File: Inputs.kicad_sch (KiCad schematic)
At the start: 2 parts, among them J15 Digital Inputs

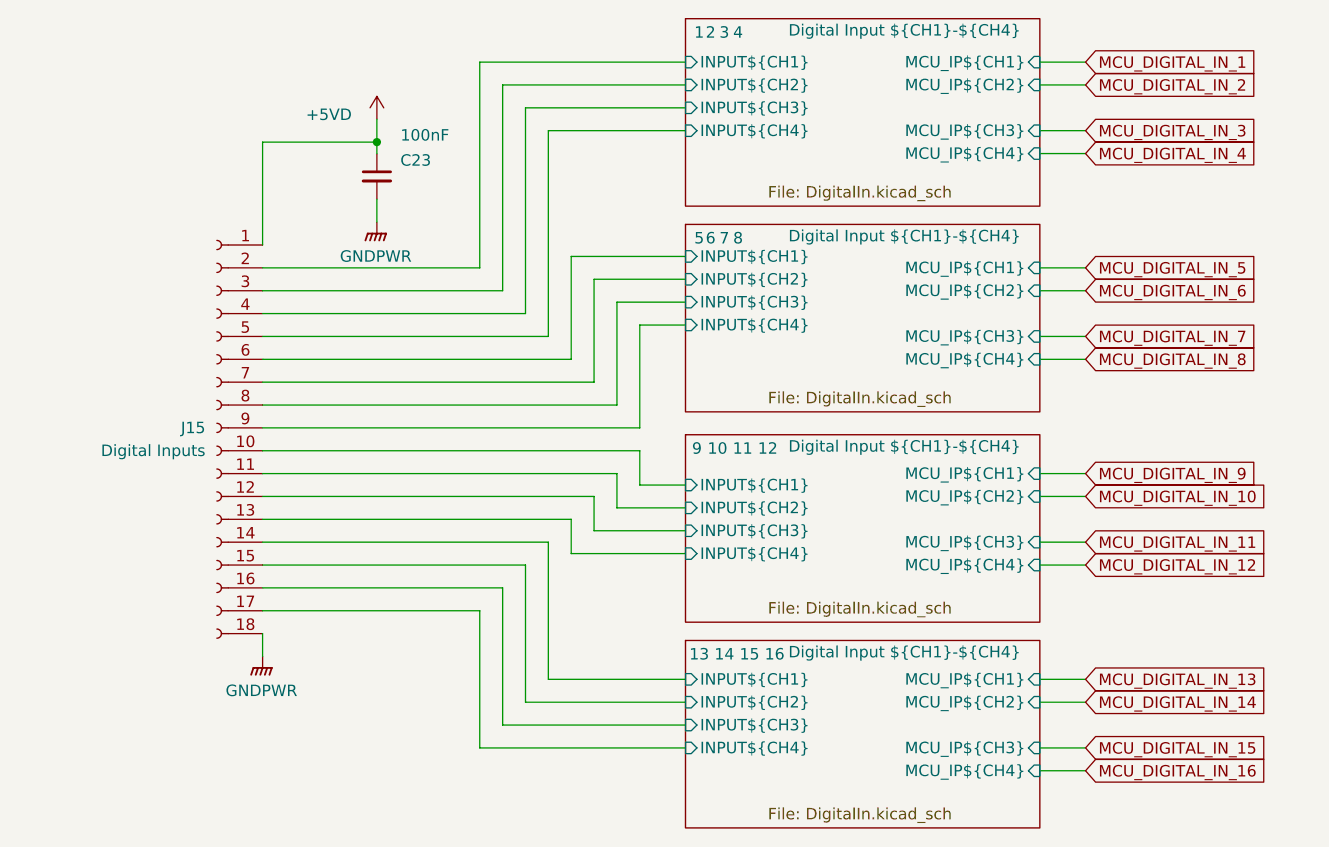
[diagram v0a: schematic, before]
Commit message: Renumbered IO to start at 0 to match firmware
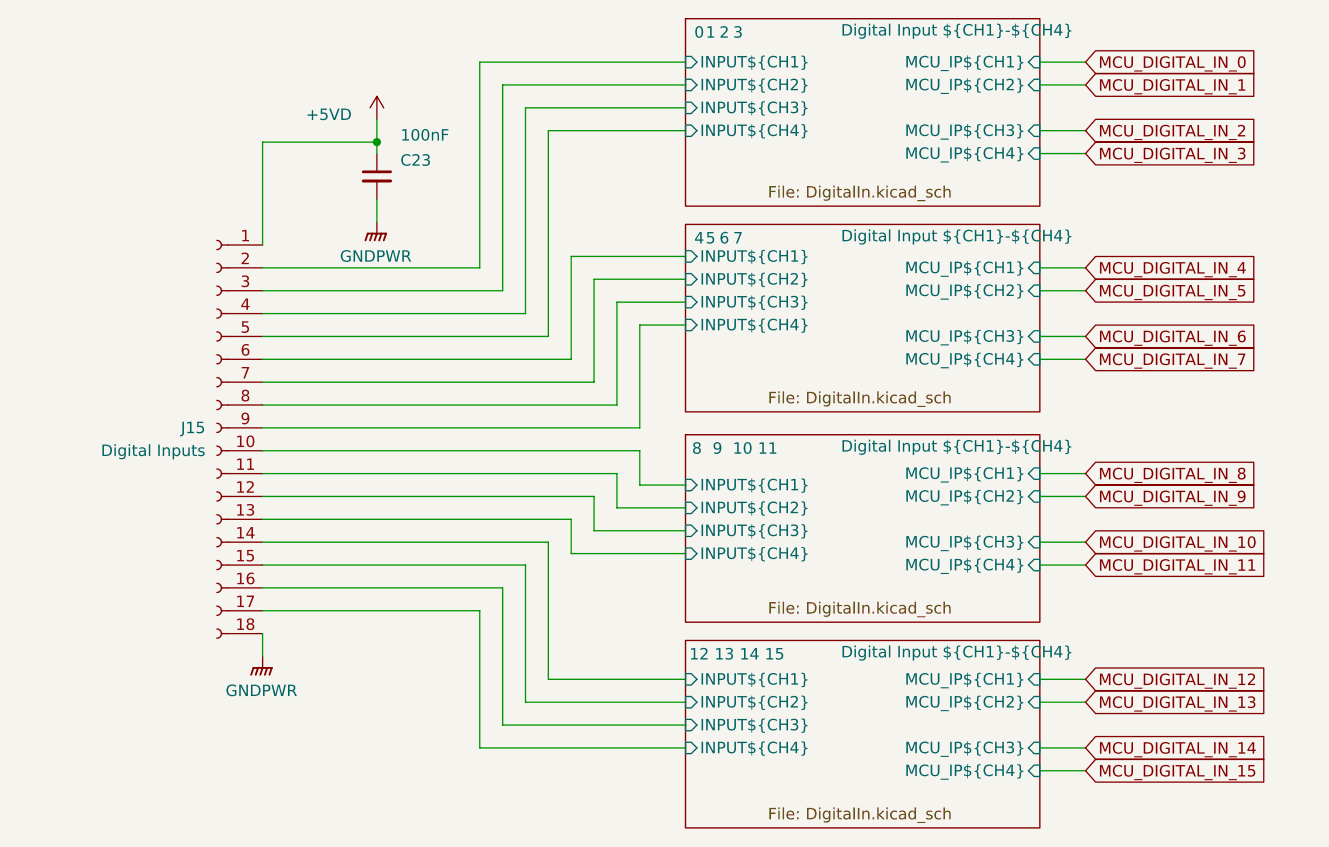
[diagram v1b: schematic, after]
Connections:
- net Digital Input ${CH1}-${CH4}/INPUT${CH1} is gone; now on net Digital Input ${CH1}-${CH4}/INPUT${CH1}: J15.6 (Pin_6)
- net Digital Input ${CH1}-${CH4}/INPUT${CH2} is gone; now on net Digital Input ${CH1}-${CH4}/INPUT${CH2}: J15.7 (Pin_7)
- net Digital Input ${CH1}-${CH4}/INPUT${CH3} is gone; now on net Digital Input ${CH1}-${CH4}/INPUT${CH3}: J15.8 (Pin_8)
- net Digital Input ${CH1}-${CH4}/INPUT${CH4} is gone; now on net Digital Input ${CH1}-${CH4}/INPUT${CH4}: J15.9 (Pin_9)
- net Digital Input ${CH1}-${CH4}/INPUT${CH1}: no longer J15.10 (Pin_10)
- net Digital Input ${CH1}-${CH4}/INPUT${CH2}: no longer J15.11 (Pin_11)
- net Digital Input ${CH1}-${CH4}/INPUT${CH3}: no longer J15.12 (Pin_12)
- net Digital Input ${CH1}-${CH4}/INPUT${CH4}: no longer J15.13 (Pin_13)
- new net Digital Input ${CH1}-${CH4}/INPUT${CH1}: J15.10 (Pin_10)
- new net Digital Input ${CH1}-${CH4}/INPUT${CH2}: J15.11 (Pin_11)
- new net Digital Input ${CH1}-${CH4}/INPUT${CH3}: J15.12 (Pin_12)
- new net Digital Input ${CH1}-${CH4}/INPUT${CH4}: J15.13 (Pin_13)

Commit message: more BOM consolidation. Switched out IO for vertical toolless wire to board terminals and added footprints. Put new isolated ground plane on board.
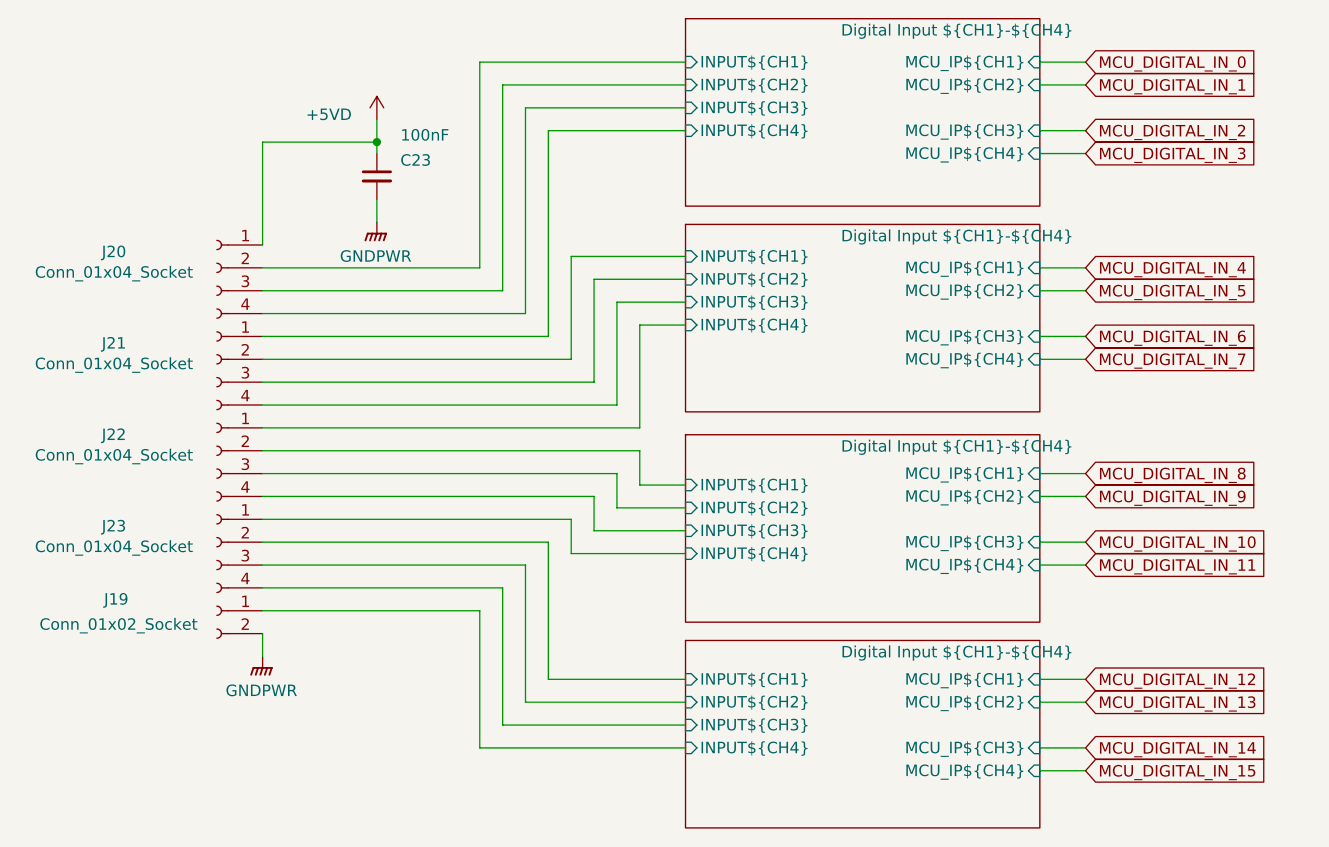
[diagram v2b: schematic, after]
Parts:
- removed J15: Digital Inputs, EBWA_06_A:CONN_EBWA-18-A_ADM, symbol Connector:Conn_01x18_Socket
- added J19: Conn_01x02_Socket, Amphenol QT:QT02ADP83V0000G, symbol Connector:Conn_01x02_Socket
- added J20, J21, J22, J23: Conn_01x04_Socket, Amphenol QT:QT04ADP83V0000G, symbol Connector:Conn_01x04_Socket
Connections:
- net +5VD: now also J20.1 (Pin_1)
- net Digital Input ${CH1}-${CH4}/INPUT${CH1}: now also J21.2 (Pin_2)
- net Digital Input ${CH1}-${CH4}/INPUT${CH2}: now also J21.3 (Pin_3)
- net Digital Input ${CH1}-${CH4}/INPUT${CH3}: now also J21.4 (Pin_4)
- net Digital Input ${CH1}-${CH4}/INPUT${CH4}: now also J21.1 (Pin_1)
- net GNDPWR: now also J19.2 (Pin_2)
- new net Digital Input ${CH1}-${CH4}/INPUT${CH1}: J23.2 (Pin_2)
- new net Digital Input ${CH1}-${CH4}/INPUT${CH1}: J20.2 (Pin_2)
- new net Digital Input ${CH1}-${CH4}/INPUT${CH1}: J22.2 (Pin_2)
- new net Digital Input ${CH1}-${CH4}/INPUT${CH2}: J23.3 (Pin_3)
- new net Digital Input ${CH1}-${CH4}/INPUT${CH2}: J20.3 (Pin_3)
- new net Digital Input ${CH1}-${CH4}/INPUT${CH2}: J22.3 (Pin_3)
- new net Digital Input ${CH1}-${CH4}/INPUT${CH3}: J23.4 (Pin_4)
- new net Digital Input ${CH1}-${CH4}/INPUT${CH3}: J20.4 (Pin_4)
- new net Digital Input ${CH1}-${CH4}/INPUT${CH3}: J22.4 (Pin_4)
- new net Digital Input ${CH1}-${CH4}/INPUT${CH4}: J23.1 (Pin_1)
- new net Digital Input ${CH1}-${CH4}/INPUT${CH4}: J19.1 (Pin_1)
- new net Digital Input ${CH1}-${CH4}/INPUT${CH4}: J22.1 (Pin_1)

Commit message: New PSU designs + footprints assigned. Changes to board shape to make room for new components. BOM consolidation of supplimentary file
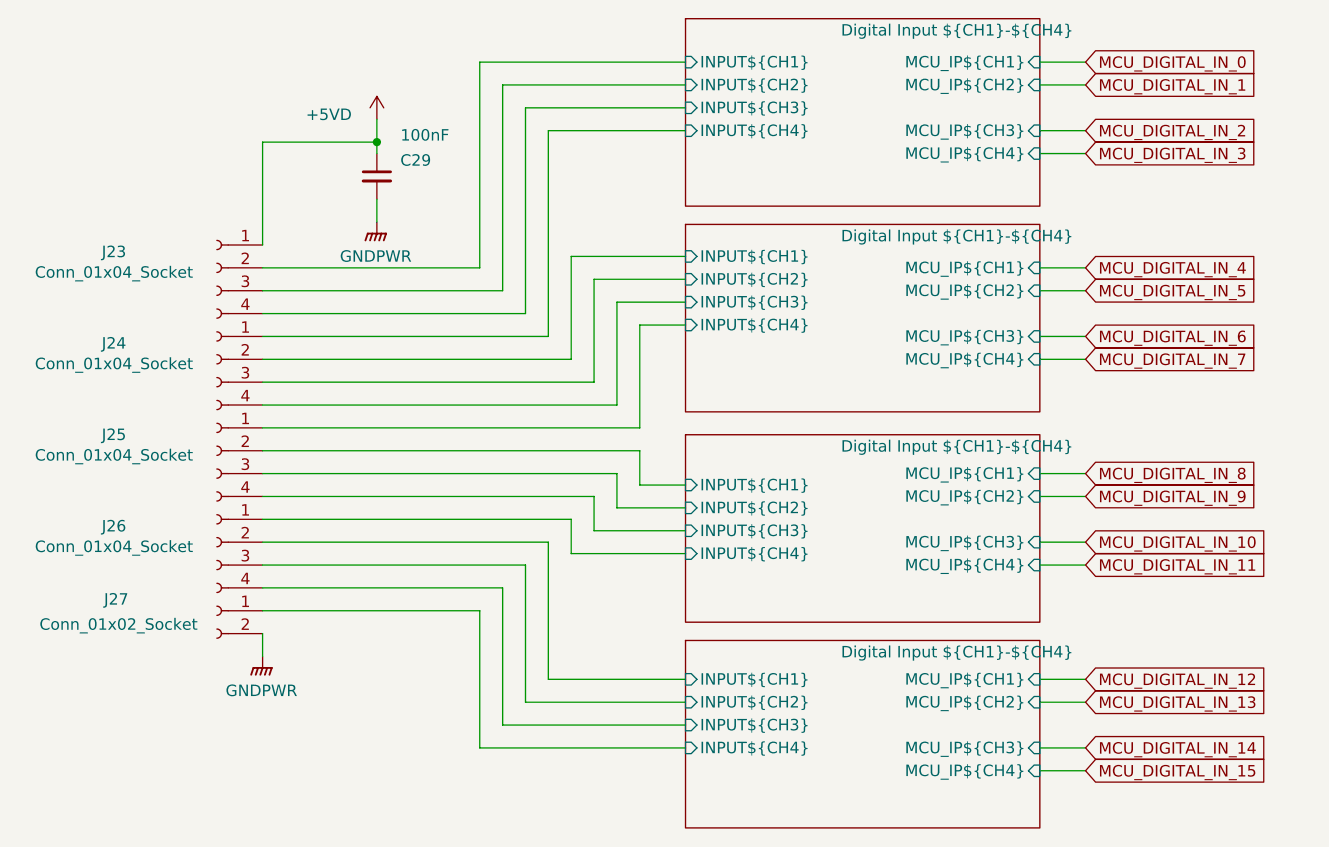
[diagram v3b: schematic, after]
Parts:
- J23: renamed from J20; Digikey Part Number 1818-QT02ADP83V0000G-ND -> 1818-QT04ADP83V0000G-ND; Digikey URL https://www.digikey.com.au/en/products/detail/amphenol-anytek/QT02ADP83V0000G/25618889 -> https://www.digikey.com.au/en/products/detail/amphenol-anytek/QT04ADP83V0000G/25618782
- J24: renamed from J21; Digikey Part Number 1818-QT02ADP83V0000G-ND -> 1818-QT04ADP83V0000G-ND; Digikey URL https://www.digikey.com.au/en/products/detail/amphenol-anytek/QT02ADP83V0000G/25618889 -> https://www.digikey.com.au/en/products/detail/amphenol-anytek/QT04ADP83V0000G/25618782
- J25: renamed from J22; Digikey Part Number 1818-QT02ADP83V0000G-ND -> 1818-QT04ADP83V0000G-ND; Digikey URL https://www.digikey.com.au/en/products/detail/amphenol-anytek/QT02ADP83V0000G/25618889 -> https://www.digikey.com.au/en/products/detail/amphenol-anytek/QT04ADP83V0000G/25618782
- J26: renamed from J23; Digikey Part Number 1818-QT02ADP83V0000G-ND -> 1818-QT04ADP83V0000G-ND; Digikey URL https://www.digikey.com.au/en/products/detail/amphenol-anytek/QT02ADP83V0000G/25618889 -> https://www.digikey.com.au/en/products/detail/amphenol-anytek/QT04ADP83V0000G/25618782
- J27: renamed from J19; Digikey Part Number 1818-QT04ADP83V0000G-ND -> 1818-QT02ADP83V0000G-ND; Digikey URL https://www.digikey.com.au/en/products/detail/amphenol-anytek/QT04ADP83V0000G/25618782 -> https://www.digikey.com.au/en/products/detail/amphenol-anytek/QT02ADP83V0000G/25618889
- renumbered C23 to C29
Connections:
- net Digital Input ${CH1}-${CH4}/INPUT${CH1} is gone; now on net Digital Input ${CH1}-${CH4}/INPUT${CH1}: J24.2 (Pin_2)
- net Digital Input ${CH1}-${CH4}/INPUT${CH2} is gone; now on net Digital Input ${CH1}-${CH4}/INPUT${CH2}: J24.3 (Pin_3)
- net Digital Input ${CH1}-${CH4}/INPUT${CH3} is gone; now on net Digital Input ${CH1}-${CH4}/INPUT${CH3}: J24.4 (Pin_4)
- net Digital Input ${CH1}-${CH4}/INPUT${CH4} is gone; now on net Digital Input ${CH1}-${CH4}/INPUT${CH4}: J24.1 (Pin_1)
- net Digital Input ${CH1}-${CH4}/INPUT${CH1}: no longer J26.2 (Pin_2)
- net Digital Input ${CH1}-${CH4}/INPUT${CH2}: no longer J26.3 (Pin_3)
- net Digital Input ${CH1}-${CH4}/INPUT${CH3}: no longer J26.4 (Pin_4)
- net Digital Input ${CH1}-${CH4}/INPUT${CH4}: no longer J26.1 (Pin_1)
- new net Digital Input ${CH1}-${CH4}/INPUT${CH1}: J26.2 (Pin_2)
- new net Digital Input ${CH1}-${CH4}/INPUT${CH2}: J26.3 (Pin_3)
- new net Digital Input ${CH1}-${CH4}/INPUT${CH3}: J26.4 (Pin_4)
- new net Digital Input ${CH1}-${CH4}/INPUT${CH4}: J26.1 (Pin_1)
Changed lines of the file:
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@@
 		(on_board yes)
 		(dnp no)
-		(property "Reference" "J23"
+		(property "Reference" "J26"
 			(at 80.01 104.902 0)
 			(effects
@@
 			)
 		)
-		(property "Digikey Part Number" "1818-QT02ADP83V0000G-ND"
+		(property "Digikey Part Number" "1818-QT04ADP83V0000G-ND"
 			(at 91.44 106.68 0)
 			(effects
@@
 			)
 		)
-		(property "Digikey URL" "https://www.digikey.com.au/en/products/detail/amphenol-anytek/QT02ADP83V0000G/25618889"
+		(property "Digikey URL" "https://www.digikey.com.au/en/products/detail/amphenol-anytek/QT04ADP83V0000G/25618782"
 			(at 91.44 106.68 0)
 			(effects
@@
 			(project "Remora Nucleo F446ZE Hat"
 				(path "/5473abc6-7b93-43cc-a401-f691c4d7d7cf/181d5939-8311-41b3-8216-f7233e3a75eb"
-					(reference "J23")
+					(reference "J26")
 					(unit 1)
 				)
@@
 		(dnp no)
 		(fields_autoplaced yes)
-		(property "Reference" "#PWR0133"
+		(property "Reference" "#PWR0202"
 			(at 96.52 124.46 0)
 			(effects
@@
 			(project "Remora Nucleo F446ZE Hat"
 				(path "/5473abc6-7b93-43cc-a401-f691c4d7d7cf/181d5939-8311-41b3-8216-f7233e3a75eb"
-					(reference "#PWR0133")
+					(reference "#PWR0202")
 					(unit 1)
 				)
@@
 		(on_board yes)
 		(dnp no)
-		(property "Reference" "#PWR0134"
+		(property "Reference" "#PWR0203"
 			(at 109.22 63.5 0)
 			(effects
@@
 			(project "Remora Nucleo F446ZE Hat"
 				(path "/5473abc6-7b93-43cc-a401-f691c4d7d7cf/181d5939-8311-41b3-8216-f7233e3a75eb"
-					(reference "#PWR0134")
+					(reference "#PWR0203")
 					(unit 1)
 				)
@@
 		(on_board yes)
 		(dnp no)
-		(property "Reference" "J20"
+		(property "Reference" "J23"
 			(at 80.01 74.422 0)
 			(effects
@@
 			)
 		)
-		(property "Digikey Part Number" "1818-QT02ADP83V0000G-ND"
+		(property "Digikey Part Number" "1818-QT04ADP83V0000G-ND"
 			(at 91.44 76.2 0)
 			(effects
@@
 			)
 		)
-		(property "Digikey URL" "https://www.digikey.com.au/en/products/detail/amphenol-anytek/QT02ADP83V0000G/25618889"
+		(property "Digikey URL" "https://www.digikey.com.au/en/products/detail/amphenol-anytek/QT04ADP83V0000G/25618782"
 			(at 91.44 76.2 0)
 			(effects
@@
 			(project "Remora Nucleo F446ZE Hat"
 				(path "/5473abc6-7b93-43cc-a401-f691c4d7d7cf/181d5939-8311-41b3-8216-f7233e3a75eb"
-					(reference "J20")
+					(reference "J23")
 					(unit 1)
 				)
@@
 		(on_board yes)
 		(dnp no)
-		(property "Reference" "C23"
+		(property "Reference" "C29"
 			(at 113.538 64.262 0)
 			(effects
@@
 			(project "Remora Nucleo F446ZE Hat"
 				(path "/5473abc6-7b93-43cc-a401-f691c4d7d7cf/181d5939-8311-41b3-8216-f7233e3a75eb"
-					(reference "C23")
+					(reference "C29")
 					(unit 1)
 				)
@@
 		(dnp no)
 		(fields_autoplaced yes)
-		(property "Reference" "#PWR0135"
+		(property "Reference" "#PWR0204"
 			(at 109.22 76.2 0)
 			(effects
@@
 			(project "Remora Nucleo F446ZE Hat"
 				(path "/5473abc6-7b93-43cc-a401-f691c4d7d7cf/181d5939-8311-41b3-8216-f7233e3a75eb"
-					(reference "#PWR0135")
+					(reference "#PWR0204")
 					(unit 1)
 				)
@@
 		(on_board yes)
 		(dnp no)
-		(property "Reference" "J19"
+		(property "Reference" "J27"
 			(at 80.264 113.03 0)
 			(effects
@@
 			)
 		)
-		(property "Digikey Part Number" "1818-QT04ADP83V0000G-ND"
+		(property "Digikey Part Number" "1818-QT02ADP83V0000G-ND"
 			(at 91.44 114.3 0)
 			(effects
@@
 			)
 		)
-		(property "Digikey URL" "https://www.digikey.com.au/en/products/detail/amphenol-anytek/QT04ADP83V0000G/25618782"
+		(property "Digikey URL" "https://www.digikey.com.au/en/products/detail/amphenol-anytek/QT02ADP83V0000G/25618889"
 			(at 91.44 114.3 0)
 			(effects
@@
 			(project "Remora Nucleo F446ZE Hat"
 				(path "/5473abc6-7b93-43cc-a401-f691c4d7d7cf/181d5939-8311-41b3-8216-f7233e3a75eb"
-					(reference "J19")
+					(reference "J27")
 					(unit 1)
 				)
@@
 		(on_board yes)
 		(dnp no)
-		(property "Reference" "J22"
+		(property "Reference" "J25"
 			(at 80.01 94.742 0)
 			(effects
@@
 			)
 		)
-		(property "Digikey Part Number" "1818-QT02ADP83V0000G-ND"
+		(property "Digikey Part Number" "1818-QT04ADP83V0000G-ND"
 			(at 91.44 96.52 0)
 			(effects
@@
 			)
 		)
-		(property "Digikey URL" "https://www.digikey.com.au/en/products/detail/amphenol-anytek/QT02ADP83V0000G/25618889"
+		(property "Digikey URL" "https://www.digikey.com.au/en/products/detail/amphenol-anytek/QT04ADP83V0000G/25618782"
 			(at 91.44 96.52 0)
 			(effects
@@
 			(project "Remora Nucleo F446ZE Hat"
 				(path "/5473abc6-7b93-43cc-a401-f691c4d7d7cf/181d5939-8311-41b3-8216-f7233e3a75eb"
-					(reference "J22")
+					(reference "J25")
 					(unit 1)
 				)
@@
 		(on_board yes)
 		(dnp no)
-		(property "Reference" "J21"
+		(property "Reference" "J24"
 			(at 80.01 84.582 0)
 			(effects
@@
 			)
 		)
-		(property "Digikey Part Number" "1818-QT02ADP83V0000G-ND"
+		(property "Digikey Part Number" "1818-QT04ADP83V0000G-ND"
 			(at 91.44 86.36 0)
 			(effects
@@
 			)
 		)
-		(property "Digikey URL" "https://www.digikey.com.au/en/products/detail/amphenol-anytek/QT02ADP83V0000G/25618889"
+		(property "Digikey URL" "https://www.digikey.com.au/en/products/detail/amphenol-anytek/QT04ADP83V0000G/25618782"
 			(at 91.44 86.36 0)
 			(effects
@@
 			(project "Remora Nucleo F446ZE Hat"
 				(path "/5473abc6-7b93-43cc-a401-f691c4d7d7cf/181d5939-8311-41b3-8216-f7233e3a75eb"
-					(reference "J21")
-					(unit 1)
-				)
+					(reference "J24")
+					(unit 1)
+				)
